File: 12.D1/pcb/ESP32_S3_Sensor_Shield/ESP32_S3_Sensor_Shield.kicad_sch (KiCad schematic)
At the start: 9 parts, among them J1 GY521, J2 GY273, U1 ESP32-S3

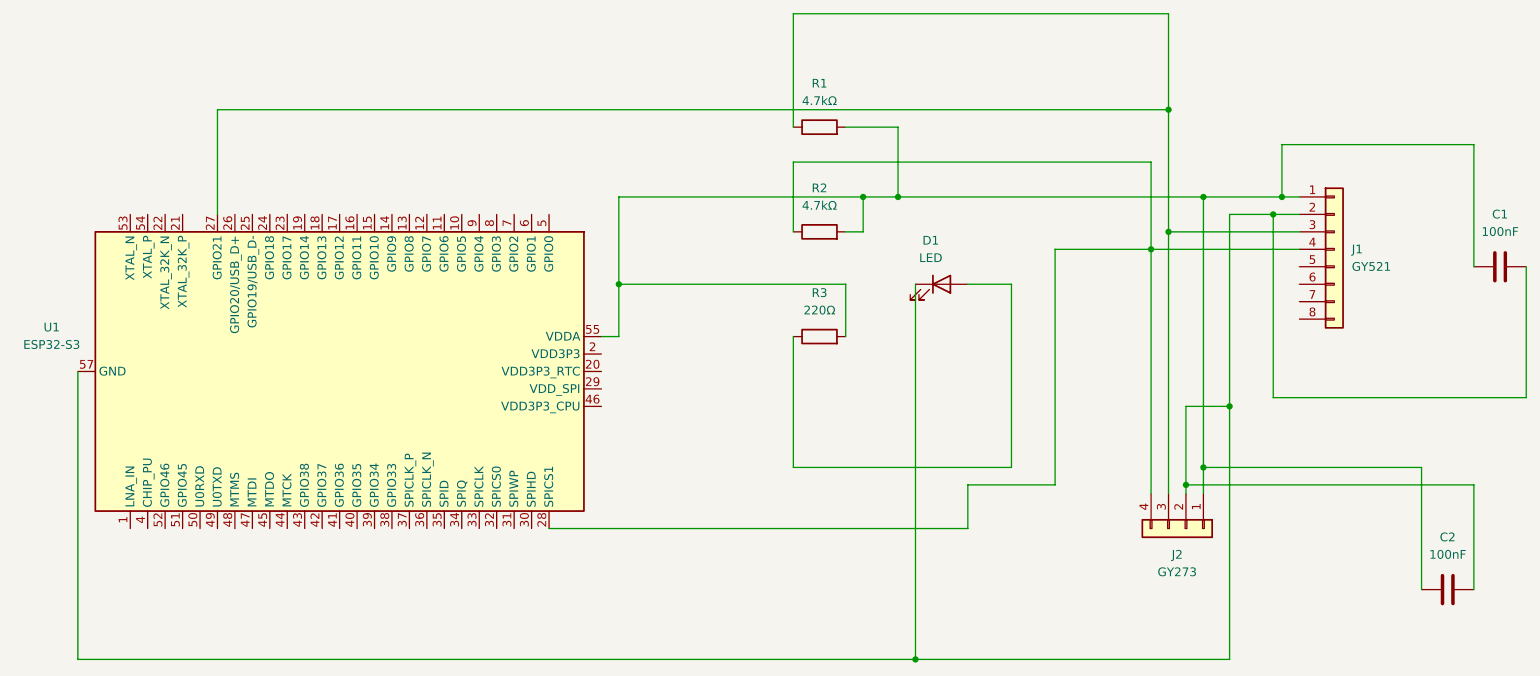
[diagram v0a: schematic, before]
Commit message: 完成12.D2全量交付文件归档： 1. D1存放KiCad PCB源工程，完成布线、铺铜、DRC校验 2. D2包含数据集data、预处理code、标定文档docs、PCB打板Gerber包prb_output、截图screenshots 全套硬件标定+人体识别数据文件整理完毕
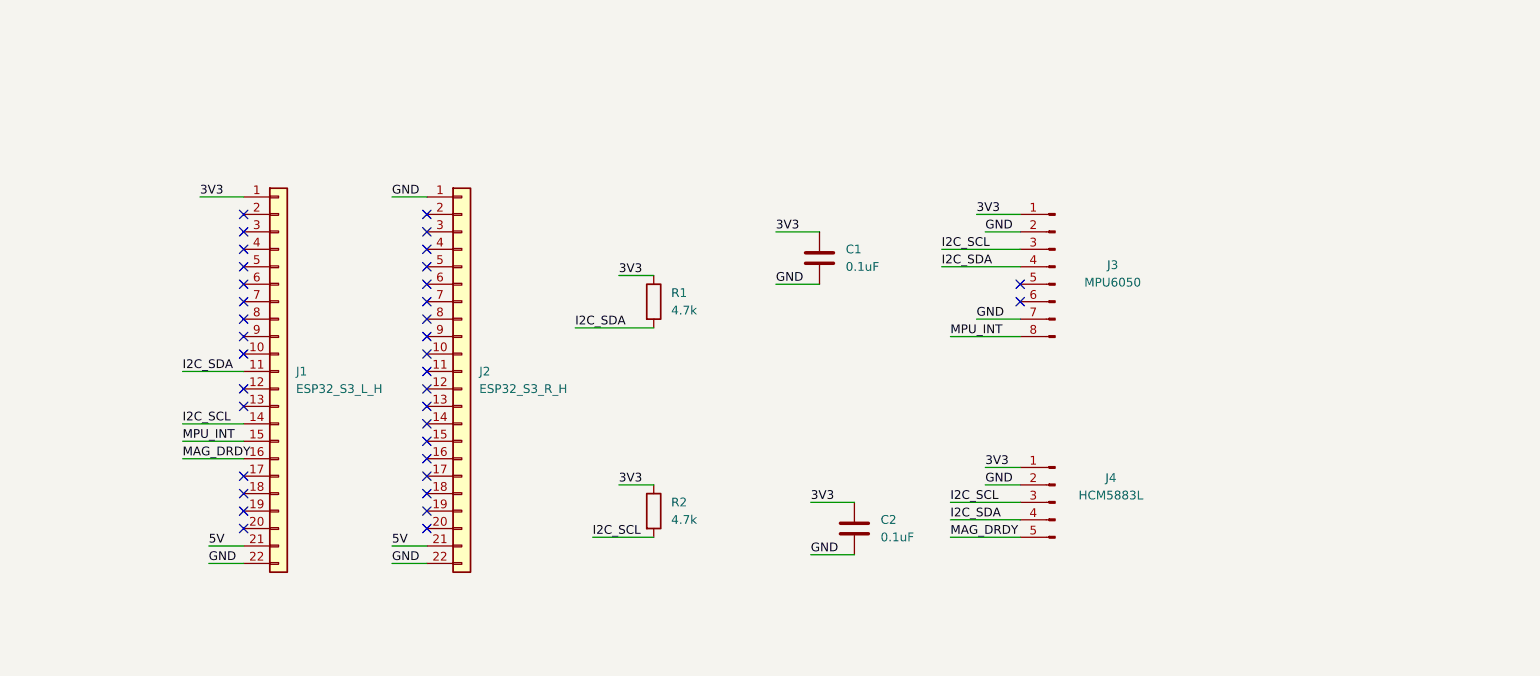
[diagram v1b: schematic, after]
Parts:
- removed D1: LED, symbol Device:LED
- removed J1: GY521, symbol Connector_Generic:Conn_01x08
- removed J2: GY273, symbol Connector_Generic:Conn_01x04
- removed R3: 220Ω, symbol Device:R
- removed U1: ESP32-S3, Package_DFN_QFN:QFN-56-1EP_7x7mm_P0.4mm_EP4x4mm, symbol MCU_Espressif:ESP32-S3
- added J1: ESP32_S3_L_H, Connector_PinSocket_2.54mm:PinSocket_1x22_P2.54mm_Vertical, symbol Connector_Generic:Conn_01x22
- added J2: ESP32_S3_R_H, Connector_PinSocket_2.54mm:PinSocket_1x22_P2.54mm_Vertical, symbol Connector_Generic:Conn_01x22
- added J3: MPU6050, Connector_PinHeader_2.54mm:PinHeader_1x08_P2.54mm_Vertical, symbol Connector:Conn_01x08_Pin
- added J4: HCM5883L, Connector_PinHeader_2.54mm:PinHeader_1x05_P2.54mm_Vertical, symbol Connector:Conn_01x05_Pin
- C1, C2: value 100nF -> 0.1uF; footprint (none) -> Capacitor_SMD:C_0805_2012Metric
- R1, R2: value 4.7kΩ -> 4.7k; footprint (none) -> Resistor_SMD:R_0805_2012Metric
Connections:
- net GND: now reaches C1.2, C2.2
- net GND: now also J1.22 (Pin_22), J2.1 (Pin_1), J2.22 (Pin_22), J3.2 (Pin_2), J3.7 (Pin_7), J4.2 (Pin_2)
- net 3V3: now reaches C1.1, C2.1
- net 3V3: now also R1.1, R2.1, J1.1 (Pin_1), J3.1 (Pin_1), J4.1 (Pin_1); no longer R1.2, R2.2
- new net 5V: J1.21 (Pin_21), J2.21 (Pin_21)
- new net I2C_SCL: J1.14 (Pin_14), J3.3 (Pin_3), J4.3 (Pin_3), R2.2
- new net I2C_SDA: J1.11 (Pin_11), J3.4 (Pin_4), J4.4 (Pin_4), R1.2
- new net MAG_DRDY: J1.16 (Pin_16), J4.5 (Pin_5)
- new net MPU_INT: J1.15 (Pin_15), J3.8 (Pin_8)
- no-connect marks 0 -> 36

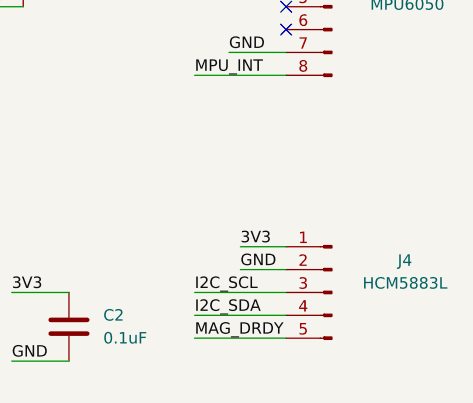
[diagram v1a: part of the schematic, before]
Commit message: 12.D1更新PCB原理图与配套文档；12.D2完成全套传感器标定： 1. 清理self_raw多余嵌套空目录； 2. 生成3被试6类人体活动raw/calibrated两套数据集； 3. 产出calib_params.json、标定报告.md、标定前后对比图； 4. 新增数据集生成、绘图Python脚本； 5. 清理zip压缩包、KiCad临时锁定文件。
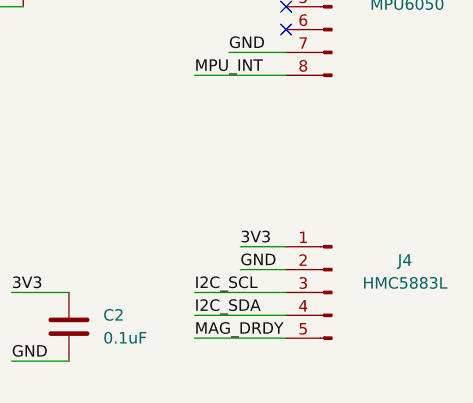
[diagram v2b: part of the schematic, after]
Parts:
- J4: value HCM5883L -> HMC5883L
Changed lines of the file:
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@@
 			)
 		)
-		(property "Value" "HCM5883L"
+		(property "Value" "HMC5883L"
 			(at 169.418 99.314 0)
 			(show_name no)
